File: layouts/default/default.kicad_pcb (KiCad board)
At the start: 2 copper layers, 120 x 130 mm, 87 parts

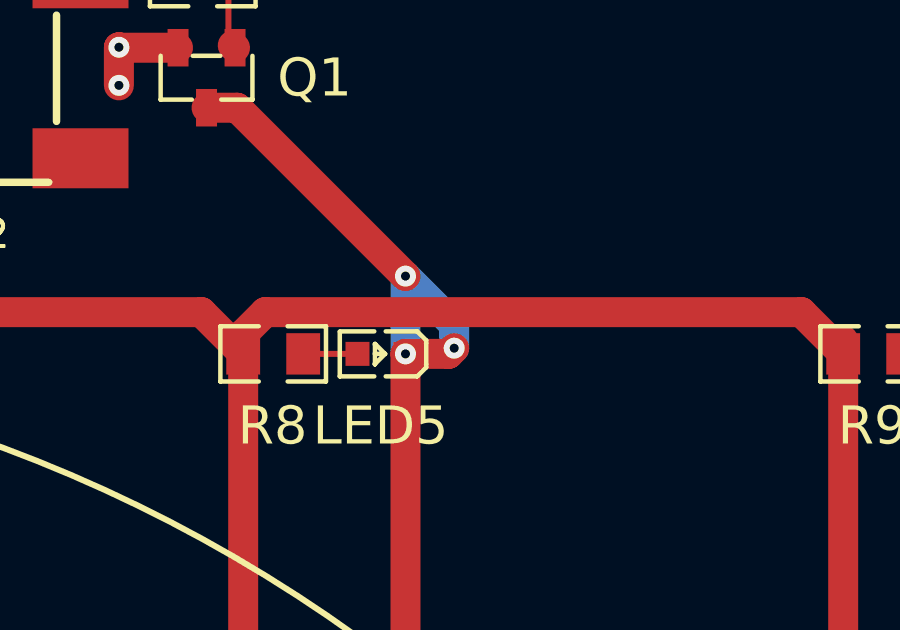
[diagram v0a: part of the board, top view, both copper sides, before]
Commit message: fix a dfm error about placing a via directly under a pad (lead to hole distance)
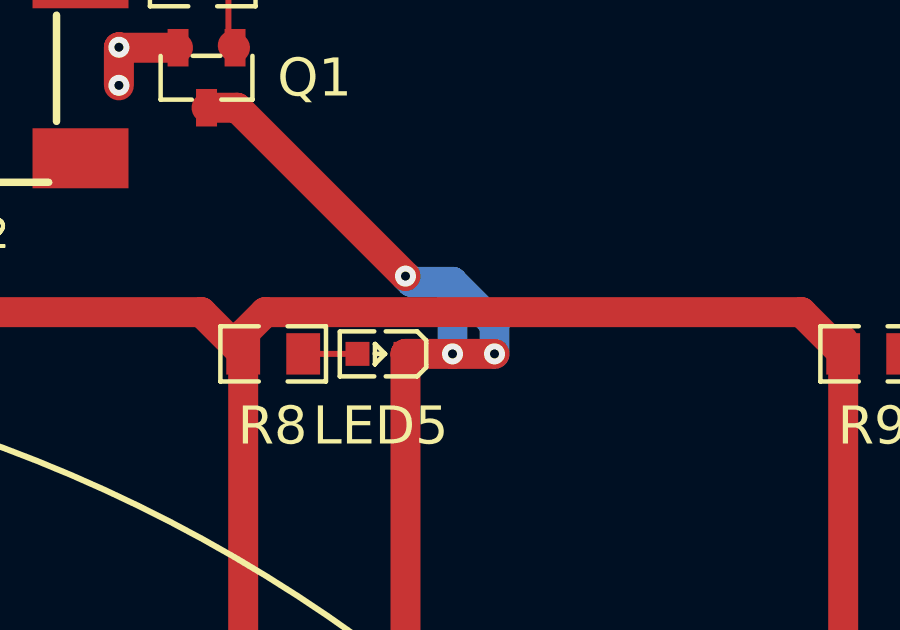
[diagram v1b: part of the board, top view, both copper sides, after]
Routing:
- net K: track 804.1 -> 806.7 mm
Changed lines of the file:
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@@
+	)
+	(segment
+		(start 90.8325 20)
+		(end 92.4 20)
+		(width 1)
+		(layer "F.Cu")
+		(net 21)
 	)
 	(segment
@@
 		(start 10.8325 120)
 		(end 12.6205 121.788)
+		(width 1)
+		(layer "F.Cu")
+		(net 21)
+	)
+	(segment
+		(start 92.4 20)
+		(end 93.8 20)
 		(width 1)
 		(layer "F.Cu")
@@
 	)
 	(segment
-		(start 90.8325 20)
-		(end 92.266 20)
-		(width 1)
-		(layer "F.Cu")
-		(net 21)
-	)
-	(segment
 		(start 72.2235 121.391)
 		(end 90.0435 121.391)
@@
 	)
 	(segment
-		(start 92.266 20)
-		(end 92.456 19.81)
-		(width 1)
-		(layer "F.Cu")
-		(net 21)
-	)
-	(segment
 		(start 110.0435 121.391)
 		(end 110.8325 120.602)
@@
 	)
 	(via
-		(at 92.456 19.81)
-		(size 0.7)
-		(drill 0.3)
-		(layers "F.Cu" "B.Cu")
-		(net 21)
-	)
-	(via
-		(at 90.8325 20)
+		(at 92.4 20)
 		(size 0.7)
 		(drill 0.3)
@@
 		(net 21)
 	)
-	(segment
-		(start 90.8325 17.408)
-		(end 90.8325 20)
-		(width 1)
-		(layer "B.Cu")
-		(net 21)
-	)
-	(segment
-		(start 92.456 19.0315)
+	(via
+		(at 93.8 20)
+		(size 0.7)
+		(drill 0.3)
+		(layers "F.Cu" "B.Cu")
+		(net 21)
+	)
+	(segment
+		(start 93.8 19)
+		(end 92.4 17.6)
+		(width 1)
+		(layer "B.Cu")
+		(net 21)
+	)
+	(segment
+		(start 92.4 17.6)
+		(end 91.0245 17.6)
+		(width 1)
+		(layer "B.Cu")
+		(net 21)
+	)
+	(segment
+		(start 91.0245 17.6)
 		(end 90.8325 17.408)
 		(width 1)
@@
 	)
 	(segment
-		(start 92.456 19.81)
-		(end 92.456 19.0315)
-		(width 1)
-		(layer "B.Cu")
+		(start 93.8 20)
+		(end 93.8 19)
+		(width 1)
+		(layer "B.Cu")
+		(net 21)
+	)
+	(segment
+		(start 92.4 20)
+		(end 92.4 17.6)
+		(width 1)
+		(layer "B.Cu")
